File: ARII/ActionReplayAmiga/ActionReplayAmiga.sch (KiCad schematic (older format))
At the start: 33 parts, among them J0 A2000_CPUSLOT_EDGE_LOGICAL, Q0 MOSFET_PCH-DMG2307L, SW0 SW_SPST, SW1 SW_SPDT, U0 TIF044 FS F74, U1 16L8-25C (TI036FF), U10 27C512-15_PLCC, U2 16L8-25C (TI036FF), U3 16L8-25C (TI036FF), U4 16L8-25C (TI042FF)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

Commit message: Added some notes, fixed VR1->VR0
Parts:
- gave numbers to parts that had none: 1
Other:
- note added: "This may be only partially correct"
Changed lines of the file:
@@
 $EndComp
 $Comp
-L SparkFun-Resistors:POTENTIOMETER-PTH-9MM-1_20W-20% VR?
+L SparkFun-Resistors:POTENTIOMETER-PTH-9MM-1_20W-20% VR0
 U 1 1 600E78A6
 P 7500 7050
-F 0 "VR?" V 7200 7050 45  0000 C CNN
-F 1 "POTENTIOMETER-PTH-9MM-1_20W-20%" V 7284 7050 45  0000 C CNN
+F 0 "VR0" V 7390 7050 45  0000 C CNN
+F 1 "POTENTIOMETER-PTH-9MM-1_20W-20%" V 7306 7050 45  0000 C CNN
 F 2 "POT-PTH-ALPS" V 7350 7050 20  0001 C CNN
 F 3 "" H 7500 7050 60  0001 C CNN
-F 4 "RES-09177" V 7379 7050 60  0000 C CNN "Field4"
+F 4 "RES-09177" V 7211 7050 60  0000 C CNN "Field4"
 	1    7500 7050
 	0    -1   -1   0
@@
 Text GLabel 3250 2250 2    50   Input ~ 0
 U0_IO8
+Text Notes 7200 6850 0    50   ~ 0
+This may be only partially correct
+Wire Notes Line
+	7050 6650 8550 6650
+Wire Notes Line
+	8550 6650 8550 7400
+Wire Notes Line
+	8550 7400 7050 7400
+Wire Notes Line
+	7050 7400 7050 6650
 $EndSCHEMATC

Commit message: U1 Completed
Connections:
- net J0_A20: now also U1.16 (IO4)
- net U0_IO8: now also U10.25 (~OE/VPP)
- net J0_A13: now reaches J0.39 (A13)
- net J0_A13: now also U1.17 (I03)
- net J0_A15: now reaches J0.43 (A15)
- net J0_A15: now also U1.19 (IO1)
- net U1_IO7: now reaches U1.13 (IO7)
- net U0_IO7: now reaches U3.5 (I5)
- no-connect marks 31 -> 32
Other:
- note added: "NC????"
- note added: "Pins 12,19 on 16L8-25C \nare Tri-State Output"
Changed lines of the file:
@@
-$EndComp
-$Comp
-L SparkFun-Capacitors:10UF-POLAR-RADIAL-2.5MM-25V-20% C5
-U 1 1 5FA83977
-P 5150 7250
-F 0 "C5" H 5278 7295 45  0000 L CNN
-F 1 "10UF-POLAR-RADIAL-2.5MM-25V-20%" H 5278 7211 45  0000 L CNN
-F 2 "CPOL-RADIAL-2.5MM-5MM" H 5150 7500 20  0001 C CNN
-F 3 "" H 5150 7250 50  0001 C CNN
-F 4 "CAP-08440" H 5278 7116 60  0000 L CNN "Field4"
-	1    5150 7250
-	1    0    0    -1
 $EndComp
 $Comp
@@
 	5000 9600 5400 9600
 Wire Wire Line
-	5150 7150 5150 7050
-Wire Wire Line
 	2500 7600 2750 7600
-Wire Wire Line
-	5150 7050 7200 7050
 $Comp
 L Switch:SW_SPDT SW1
@@
 Wire Notes Line
 	7050 7400 7050 6650
+Text GLabel 4150 2350 0    50   Input ~ 0
+U0_IO8
+Text GLabel 4600 4950 2    50   Input ~ 0
+U1_IO7
+Text GLabel 6950 4700 0    50   Input ~ 0
+U0_IO7
+Text Notes 2150 4650 0    50   ~ 0
+Pins 12,19 on 16L8-25C \nare Tri-State Output
+Wire Wire Line
+	5150 7050 7200 7050
+Wire Wire Line
+	5150 7150 5150 7050
+$Comp
+L SparkFun-Capacitors:10UF-POLAR-RADIAL-2.5MM-25V-20% C5
+U 1 1 5FA83977
+P 5150 7250
+F 0 "C5" H 5278 7295 45  0000 L CNN
+F 1 "10UF-POLAR-RADIAL-2.5MM-25V-20%" H 5278 7211 45  0000 L CNN
+F 2 "CPOL-RADIAL-2.5MM-5MM" H 5150 7500 20  0001 C CNN
+F 3 "" H 5150 7250 50  0001 C CNN
+F 4 "CAP-08440" H 5278 7116 60  0000 L CNN "Field4"
+	1    5150 7250
+	1    0    0    -1
+$EndComp
+Text GLabel 4600 4650 2    50   Input ~ 0
+J0_A20
+Text Notes 2750 7650 0    50   ~ 0
+NC????
+Text GLabel 14750 2850 2    50   Input ~ 0
+J0_A13
+Text GLabel 4600 4550 2    50   Input ~ 0
+J0_A13
+NoConn ~ 4600 4450
+Text GLabel 14750 3050 2    50   Input ~ 0
+J0_A15
+Text GLabel 4600 4350 2    50   Input ~ 0
+J0_A15
 $EndSCHEMATC

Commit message: Started U2 and added board edge cuts 96x114mm Indents are 10.1mm deep and 2.8mm heigh
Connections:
- net +5V: now also U10.32 (VCC), U8.32 (VCC), U9.28 (VCC)
- net GND: now also U9.26 (A13)
- net J0_PD11: now reaches J0.71 (PD11)
- net J0_PD11: now also U2.8 (I8), U3.4 (I4)
- net U2_I3: now reaches U4.12 (IO8)
- net U2_I3: now also U2.3 (I3), U3.3 (I3)
- net U2_I4: now reaches U2.4 (I4)
- net U2_I4: now also U3.18 (IO2)
- net U2_I5: now reaches U2.5 (I5)
- net U2_I5: now also U3.17 (I03)
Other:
- note added: "NC?????"
- moved on the sheet: U1, U2, U4, U5
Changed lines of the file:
@@
 L Logic_Programmable:PAL16L8 U1
 U 1 1 5FA914A2
-P 4100 4850
-F 0 "U1" H 4100 5731 50  0000 C CNN
-F 1 "16L8-25C (TI036FF)" H 4100 5640 50  0000 C CNN
-F 2 "" H 4100 4850 50  0001 C CNN
-F 3 "https://www.digchip.com/datasheets/parts/datasheet/477/TIBPAL16L8-25CN-pdf.php" H 4100 4850 50  0001 C CNN
-	1    4100 4850
+P 3100 4850
+F 0 "U1" H 3100 5731 50  0000 C CNN
+F 1 "16L8-25C (TI036FF)" H 3100 5640 50  0000 C CNN
+F 2 "" H 3100 4850 50  0001 C CNN
+F 3 "https://www.digchip.com/datasheets/parts/datasheet/477/TIBPAL16L8-25CN-pdf.php" H 3100 4850 50  0001 C CNN
+	1    3100 4850
 	1    0    0    -1
 $EndComp
@@
 L Logic_Programmable:PAL16L8 U4
 U 1 1 5FA95522
-P 9000 4750
-F 0 "U4" H 9000 5631 50  0000 C CNN
-F 1 "16L8-25C (TI042FF)" H 9000 5540 50  0000 C CNN
-F 2 "" H 9000 4750 50  0001 C CNN
-F 3 "https://www.digchip.com/datasheets/parts/datasheet/477/TIBPAL16L8-25CN-pdf.php" H 9000 4750 50  0001 C CNN
-	1    9000 4750
+P 9400 4800
+F 0 "U4" H 9400 5681 50  0000 C CNN
+F 1 "16L8-25C (TI042FF)" H 9400 5590 50  0000 C CNN
+F 2 "" H 9400 4800 50  0001 C CNN
+F 3 "https://www.digchip.com/datasheets/parts/datasheet/477/TIBPAL16L8-25CN-pdf.php" H 9400 4800 50  0001 C CNN
+	1    9400 4800
 	1    0    0    -1
 $EndComp
@@
 L Logic_Programmable:PAL16L8 U5
 U 1 1 5FA95E85
-P 10400 4750
-F 0 "U5" H 10400 5631 50  0000 C CNN
-F 1 "16L8-25C (TI026FF)" H 10400 5540 50  0000 C CNN
-F 2 "" H 10400 4750 50  0001 C CNN
-F 3 "https://www.digchip.com/datasheets/parts/datasheet/477/TIBPAL16L8-25CN-pdf.php" H 10400 4750 50  0001 C CNN
-	1    10400 4750
-	1    0    0    -1
-$EndComp
-$Comp
-L Logic_Programmable:PAL16L8 U2
-U 1 1 5FAAF643
-P 6050 4850
-F 0 "U2" H 6050 5731 50  0000 C CNN
-F 1 "16L8-25C (TI036FF)" H 6050 5640 50  0000 C CNN
-F 2 "" H 6050 4850 50  0001 C CNN
-F 3 "https://www.digchip.com/datasheets/parts/datasheet/477/TIBPAL16L8-25CN-pdf.php" H 6050 4850 50  0001 C CNN
-	1    6050 4850
+P 11350 4750
+F 0 "U5" H 11350 5631 50  0000 C CNN
+F 1 "16L8-25C (TI026FF)" H 11350 5540 50  0000 C CNN
+F 2 "" H 11350 4750 50  0001 C CNN
+F 3 "https://www.digchip.com/datasheets/parts/datasheet/477/TIBPAL16L8-25CN-pdf.php" H 11350 4750 50  0001 C CNN
+	1    11350 4750
 	1    0    0    -1
 $EndComp
@@
 Text GLabel 10700 10000 2    50   Input ~ 0
 U1_I8
-Text GLabel 3600 5050 0    50   Input ~ 0
+Text GLabel 2600 5050 0    50   Input ~ 0
 U1_I8
 $Comp
@@
 Text GLabel 1800 7700 0    50   Input ~ 0
 U0_2CLK
-Text GLabel 4600 4850 2    50   Input ~ 0
+Text GLabel 3600 4850 2    50   Input ~ 0
 U0_2CLK
 Text GLabel 1800 8000 0    50   Input ~ 0
 U0_12PRE
-Text GLabel 4600 4750 2    50   Input ~ 0
+Text GLabel 3600 4750 2    50   Input ~ 0
 U0_12PRE
 Text GLabel 1800 7600 0    50   Input ~ 0
@@
 Text GLabel 2900 7450 1    50   Input ~ 0
 U0_1Q
-Text GLabel 3600 4550 0    50   Input ~ 0
+Text GLabel 2600 4550 0    50   Input ~ 0
 U0_1Q
 Wire Wire Line
@@
 	4750 10700 4750 10500
 Connection ~ 4750 10500
-Text GLabel 3600 4750 0    50   Input ~ 0
+Text GLabel 2600 4750 0    50   Input ~ 0
 U1_I5
 $Comp
@@
 Wire Wire Line
 	7650 8750 7750 8750
-Text GLabel 3600 4850 0    50   Input ~ 0
+Text GLabel 2600 4850 0    50   Input ~ 0
 U1_I6
 Text GLabel 8850 8250 2    50   Input ~ 0
@@
 	6750 5450 7450 5450
 Wire Wire Line
-	4100 5450 6050 5450
-Connection ~ 6050 5450
-Wire Wire Line
-	6050 5450 6750 5450
-Wire Wire Line
-	8850 4100 8850 4050
-Wire Wire Line
-	8850 4050 9000 4050
-Wire Wire Line
-	9000 4050 10400 4050
-Connection ~ 9000 4050
-Wire Wire Line
-	6050 4150 7300 4150
+	9800 4100 9800 4050
 Wire Wire Line
 	7300 4150 7300 4100
 Wire Wire Line
 	7300 4100 7450 4100
-Connection ~ 6050 4150
-Connection ~ 7450 4100
-Wire Wire Line
-	7450 4100 8850 4100
-Wire Wire Line
-	4100 4150 4650 4150
 Connection ~ 4650 4150
-Wire Wire Line
-	4650 4150 6050 4150
 Wire Wire Line
 	8400 7900 8200 7900
@@
 Wire Wire Line
 	4650 3750 4650 3650
-Wire Wire Line
-	9000 5350 10400 5350
-Text GLabel 9700 5350 3    50   Input ~ 0
+Text GLabel 10100 5400 3    50   Input ~ 0
 U4_U5_GND
 Wire Wire Line
 	4650 3350 4650 3050
 Connection ~ 4650 3350
-Text GLabel 5550 4950 0    50   Input ~ 0
-U1_I1
 Text GLabel 13050 3050 0    50   Input ~ 0
 J0_GND73
-Text GLabel 3600 4350 0    50   Input ~ 0
+Text GLabel 2600 4350 0    50   Input ~ 0
 J0_GND73
 Text GLabel 7950 4800 2    50   Input ~ 0
 J0_GND73
-Text GLabel 3600 4450 0    50   Input ~ 0
+Text GLabel 2600 4450 0    50   Input ~ 0
 J0_PD13
 Text GLabel 14750 5350 2    50   Input ~ 0
@@
 	1    0    0    -1
 $EndComp
-NoConn ~ 3600 5150
-Text GLabel 3600 5250 0    50   Input ~ 0
+NoConn ~ 2600 5150
+Text GLabel 2600 5250 0    50   Input ~ 0
 U1_I10
 Text GLabel 7950 4600 2    50   Input ~ 0
 U1_I10
-Text GLabel 5550 5250 0    50   Input ~ 0
-U1_I10
-Text GLabel 3600 4650 0    50   Input ~ 0
+Text GLabel 2600 4650 0    50   Input ~ 0
 U1_I4
 Text GLabel 7950 4700 2    50   Input ~ 0
@@
 Text GLabel 1100 7000 1    50   Input ~ 0
 U1_I7
-Text GLabel 3600 4950 0    50   Input ~ 0
+Text GLabel 2600 4950 0    50   Input ~ 0
 U1_I7
-Text GLabel 4600 5050 2    50   Input ~ 0
-U0_IO8
-Text GLabel 5550 4850 0    50   Input ~ 0
+Text GLabel 3600 5050 2    50   Input ~ 0
 U0_IO8
 Text GLabel 9300 2250 2    50   Input ~ 0
@@
 Text GLabel 4150 2350 0    50   Input ~ 0
 U0_IO8
-Text GLabel 4600 4950 2    50   Input ~ 0
+Text GLabel 3600 4950 2    50   Input ~ 0
 U1_IO7
-Text GLabel 6950 4700 0    50   Input ~ 0
-U0_IO7
-Text Notes 2150 4650 0    50   ~ 0
+Text Notes 1150 4650 0    50   ~ 0
 Pins 12,19 on 16L8-25C \nare Tri-State Output
 Wire Wire Line
@@
 	1    0    0    -1
 $EndComp
-Text GLabel 4600 4650 2    50   Input ~ 0
+Text GLabel 3600 4650 2    50   Input ~ 0
 J0_A20
 Text Notes 2750 7650 0    50   ~ 0
@@
 Text GLabel 14750 2850 2    50   Input ~ 0
 J0_A13
-Text GLabel 4600 4550 2    50   Input ~ 0
+Text GLabel 3600 4550 2    50   Input ~ 0
 J0_A13
-NoConn ~ 4600 4450
+NoConn ~ 3600 4450
 Text GLabel 14750 3050 2    50   Input ~ 0
 J0_A15
-Text GLabel 4600 4350 2    50   Input ~ 0
+Text GLabel 3600 4350 2    50   Input ~ 0
 J0_A15
+Text Notes 6250 9500 0    50   ~ 0
+NC?????
+Wire Wire Line
+	3100 4150 4650 4150
+Wire Wire Line
+	3100 5450 5700 5450
+Wire Wire Line
+	4650 4150 5700 4150
+Text GLabel 6950 4700 0    50   Input ~ 0
+U0_IO7
+Text GLabel 5200 4850 0    50   Input ~ 0
+U0_IO8
+Text GLabel 5200 5250 0    50   Input ~ 0
+U1_I10
+Text GLabel 5200 4950 0    50   Input ~ 0
+U1_I1
+$Comp
+L Logic_Programmable:PAL16L8 U2
+U 1 1 5FAAF643
+P 5700 4850
+F 0 "U2" H 5700 5731 50  0000 C CNN
+F 1 "16L8-25C (TI036FF)" H 5700 5640 50  0000 C CNN
+F 2 "" H 5700 4850 50  0001 C CNN
+F 3 "https://www.digchip.com/datasheets/parts/datasheet/477/TIBPAL16L8-25CN-pdf.php" H 5700 4850 50  0001 C CNN
+	1    5700 4850
+	1    0    0    -1
+$EndComp
+Connection ~ 5700 4150
+Connection ~ 5700 5450
+Wire Wire Line
+	5700 4150 7300 4150
+Wire Wire Line
+	5700 5450 6750 5450
+Text GLabel 5200 4550 0    50   Input ~ 0
+U2_I3
+Text GLabel 6950 4500 0    50   Input ~ 0
+U2_I3
+Text GLabel 9900 5000 2    50   Input ~ 0
+U2_I3
+Wire Wire Line
+	7450 4100 9400 4100
+Connection ~ 7450 4100
+Connection ~ 9400 4100
+Wire Wire Line
+	9400 4100 9800 4100
+Wire Wire Line
+	9800 4050 11350 4050
+Wire Wire Line
+	11350 5400 11350 5350
+Wire Wire Line
+	9400 5400 11350 5400
+$Comp
+L power:+5V #PWR?
+U 1 1 5FF40B6C
+P 4650 1050
+F 0 "#PWR?" H 4650 900 50  0001 C CNN
+F 1 "+5V" H 4665 1223 50  0000 C CNN
+F 2 "" H 4650 1050 50  0001 C CNN
+F 3 "" H 4650 1050 50  0001 C CNN
+	1    4650 1050
+	1    0    0    -1
+$EndComp
+$Comp
+L power:+5V #PWR?
+U 1 1 5FF4196F
+P 6700 1050
+F 0 "#PWR?" H 6700 900 50  0001 C CNN
+F 1 "+5V" H 6715 1223 50  0000 C CNN
+F 2 "" H 6700 1050 50  0001 C CNN
+F 3 "" H 6700 1050 50  0001 C CNN
+	1    6700 1050
+	1    0    0    -1
+$EndComp
+$Comp
+L power:+5V #PWR?
+U 1 1 5FF44F56
+P 2750 1150
+F 0 "#PWR?" H 2750 1000 50  0001 C CNN
+F 1 "+5V" H 2765 1323 50  0000 C CNN
+F 2 "" H 2750 1150 50  0001 C CNN
+F 3 "" H 2750 1150 50  0001 C CNN
+	1    2750 1150
+	1    0    0    -1
+$EndComp
+$Comp
+L power:GND #PWR?
+U 1 1 5FF48F3E
+P 3750 1450
+F 0 "#PWR?" H 3750 1200 50  0001 C CNN
+F 1 "GND" H 3755 1277 50  0000 C CNN
+F 2 "" H 3750 1450 50  0001 C CNN
+F 3 "" H 3750 1450 50  0001 C CNN
+	1    3750 1450
+	1    0    0    -1
+$EndComp
+Wire Wire Line
+	3250 1450 3750 1450
+Text GLabel 5200 4650 0    50   Input ~ 0
+U2_I4
+Text GLabel 7950 4400 2    50   Input ~ 0
+U2_I4
+Text GLabel 5200 4750 0    50   Input ~ 0
+U2_I5
+Text GLabel 7950 4500 2    50   Input ~ 0
+U2_I5
+Text GLabel 5200 5050 0    50   Input ~ 0
+J0_PD11
+Text GLabel 6950 4600 0    50   Input ~ 0
+J0_PD11
+Text GLabel 14750 5150 2    50   Input ~ 0
+J0_PD11
 $EndSCHEMATC

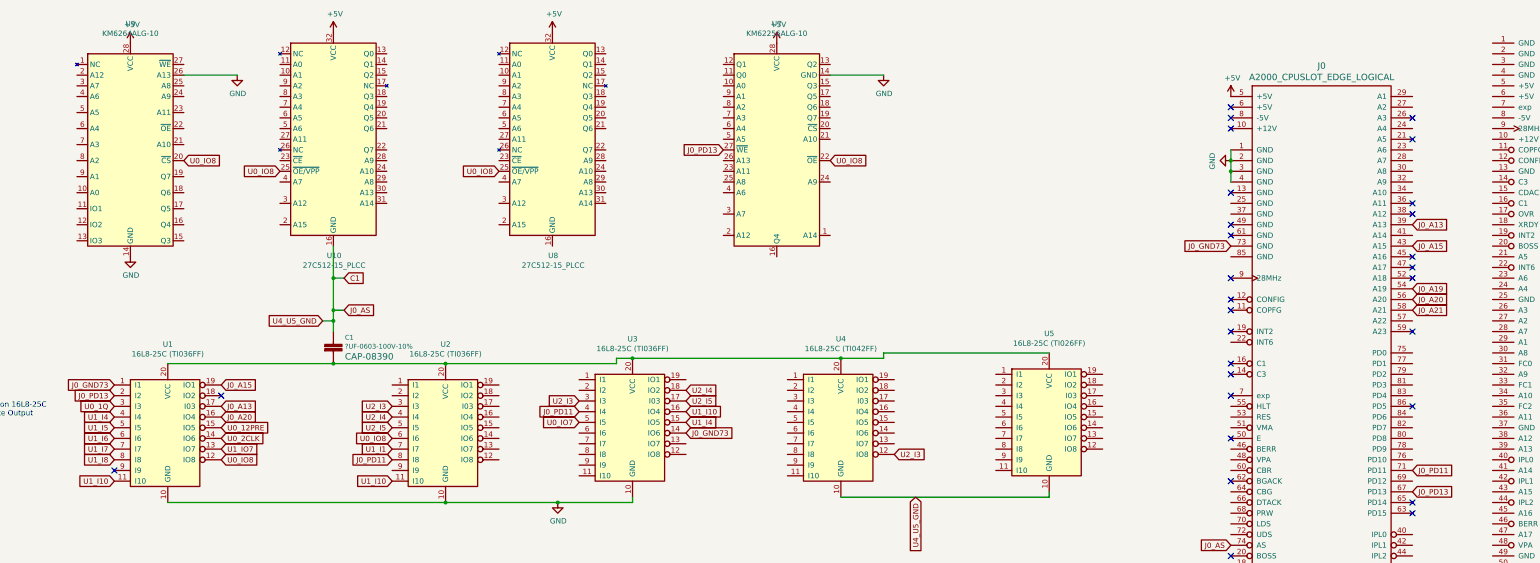
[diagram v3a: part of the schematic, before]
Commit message: Added footprints to chips Created new 2x43 header with pitch 2.54 for amiga edge connector Fixed pinout for KM6264ALG-10
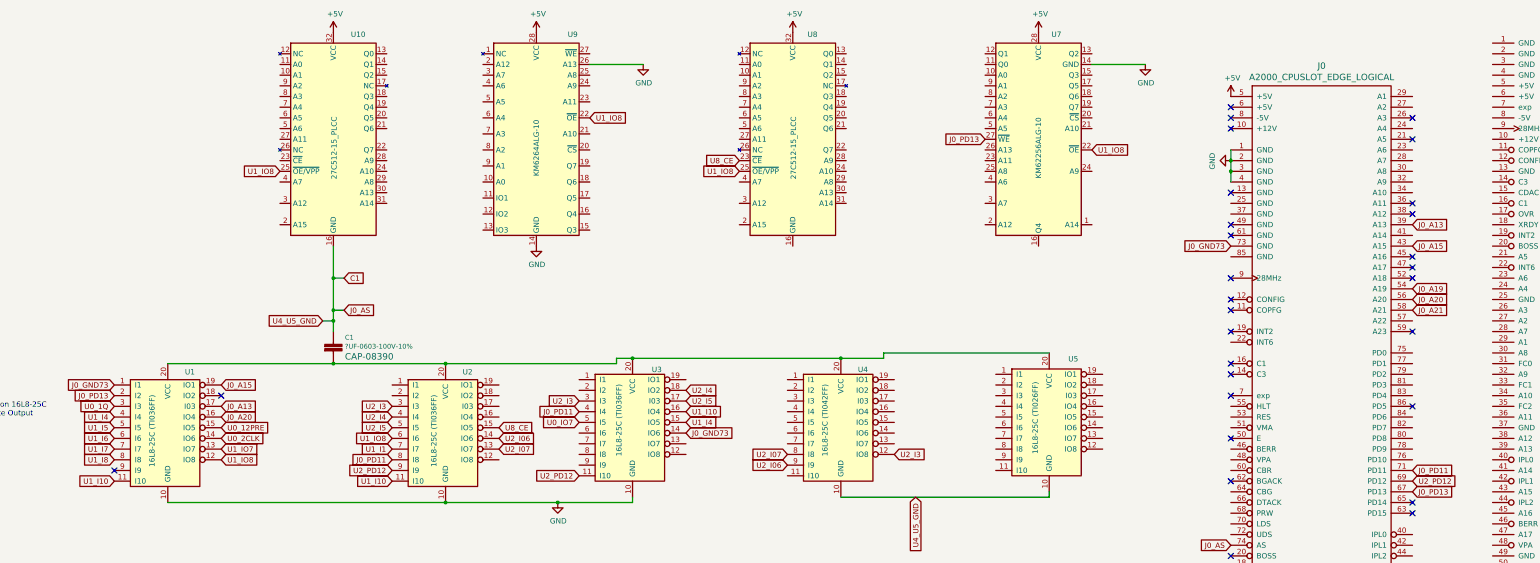
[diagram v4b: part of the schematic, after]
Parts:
- J0: footprint (none) -> ActionReplayAmiga:Pin_Header_Straight_2x43_Pitch2.54mm
- U0: footprint digikey-footprints:DIP-14_W3mm -> SMD_Packages:SOIC-14_N
- U1, U2, U3, U4, U5: footprint (none) -> Housings_LCC:PLCC-20
- U10, U8: footprint (none) -> SMD_Packages:PLCC-32
- U6: footprint DIP08 -> SMD_Packages:SOIC-8-N
- U7, U9: footprint (none) -> SMD_Packages:SOIC-28
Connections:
- net U2_PD12: now reaches J0.69 (PD12)
- net U2_PD12: now also U2.9 (I9), U3.11 (I10)
- net U2_I07: now reaches U4.8 (I8)
- net U2_I07: now also U2.13 (IO7)
- net U2_I06: now reaches U4.9 (I9)
- net U2_I06: now also U2.14 (IO6)
- net U8_CE: now reaches U2.15 (IO5)
- net U8_CE: now also U8.23 (~CE)
- net U1_IO8: now reaches U9.22 (~OE)
- net U1_IO8: now also U1.12 (IO8), U10.25 (~OE/VPP), U2.6 (I6), U7.22 (~OE), U8.25 (~OE/VPP)
- removed net U0_IO8: U1.12 (IO8), U10.25 (~OE/VPP), U2.6 (I6), U7.22 (~OE), U8.25 (~OE/VPP), U9.20 (~CS)
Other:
- moved on the sheet: U7, U8, U9
